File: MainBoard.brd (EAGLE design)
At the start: 0 parts

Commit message: Schematic for audio section
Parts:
- added C1, C10, C11, C2, C3, C4, C6, C7, C8, C9: 1µF, microbuilder:0805-NO
- added C5: 2.2u, microbuilder:0805-NO
- added J1: 22-27-2101-10, con-molex:6410-10
- added R1, R2: 10K, microbuilder:0805-NO
- added R3, R4, R5, R6: 100K, microbuilder:0805-NO
- added U1: microSD, SparkFun:MICRO-SD-SOCKET-PP
- added U2: TPA2016, tpa2016:S-PWQFN-N20
- added U3: AK4430ET, AK4430ET:16TSSOP
- added X1, X2, X3: 22-23-2021, con-molex:22-23-2021
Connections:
- new net +3V3: C10.2, C11.1, C3.2, C8.2, R1.1, R2.2, R3.2, R6.1, U1.1, U2.P$13, U3.P$11, U3.P$14
- new net AGND: C10.1, C4.1, C5.1, R4.1, R5.1, U2.P$14, U2.P$2, U2.P$3, U3.P$12
- new net GND: C11.2, C3.1, U1.6, U1.CD2, U1.GND1, U1.GND2, U2.P$21, U2.P$8
- new net I2SBICK: U3.P$5
- new net I2SLRCK: U3.P$7
- new net I2SMCLK: U3.P$4
- new net I2SSDTI: U3.P$6
- new net MMCCD: R6.2, U1.CD1
- new net MMCCS: U1.2
- new net MMCDI: U1.3
- new net MMCSCK: U1.5
- new net MMCSDO: U1.7
- new net MUTE: R1.2, R5.2, U2.P$18, U3.P$3
- new net N$1: U2.P$6, X1.1
- new net N$10: C8.1, C9.1, U3.P$15
- new net N$12: C9.2, U3.P$16
- new net N$13: C6.1, U3.P$1
- new net N$14: C6.2, U3.P$2
- new net N$15: R4.2, U3.P$8
- new net N$2: U2.P$7, X1.2
- new net N$3: U2.P$10, X2.1
- new net N$4: C2.1, U3.P$9
- new net N$5: C1.1, U3.P$10
- new net N$6: C1.2, U2.P$1
- new net N$7: C2.2, U2.P$15
- new net N$8: U2.P$9, X2.2
- new net N$9: C5.2, U3.P$13
- new net SCL: R2.1, U2.P$17
- new net SDA: R3.1, U2.P$19
- new net V+: C4.2, U2.P$11, U2.P$12, U2.P$4, U2.P$5
- new net VCC: U1.4

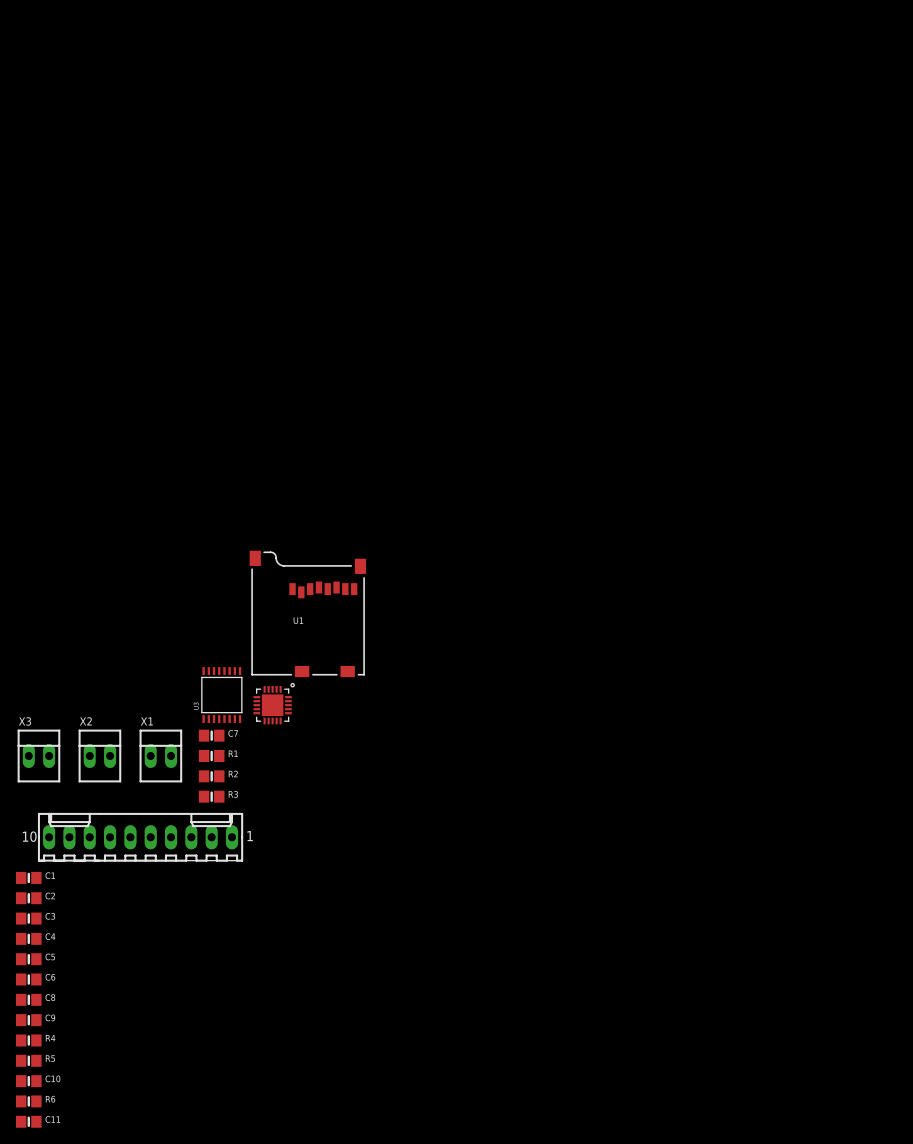
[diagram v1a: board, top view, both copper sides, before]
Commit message: Switched to SMT for power jack and headphones
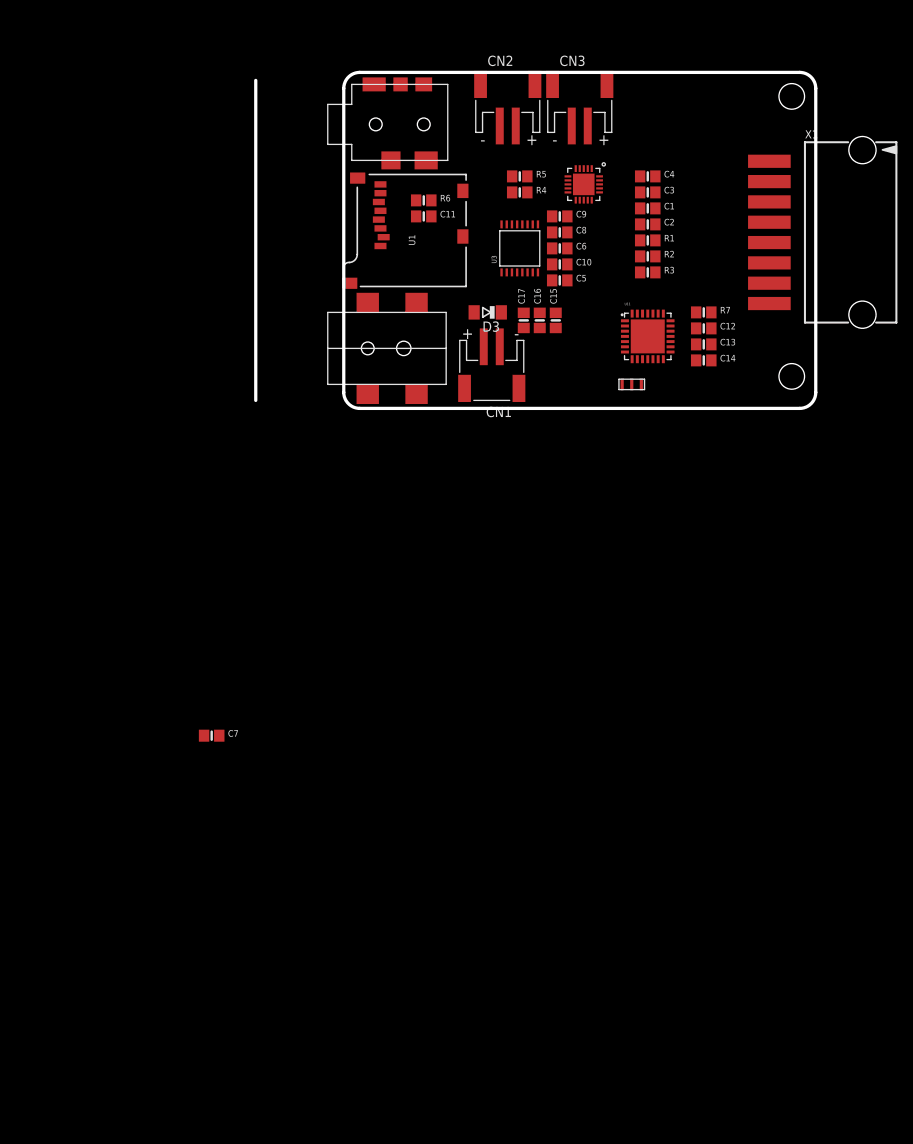
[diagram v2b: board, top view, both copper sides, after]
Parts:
- removed J1: 22-27-2101-10, con-molex:6410-10
- removed X2, X3: 22-23-2021, con-molex:22-23-2021
- added C12, C13, C14: 2.2u, microbuilder:0805-NO
- added C15, C16, C17: 1µF, microbuilder:0805-NO
- added CN1, CN2, CN3: (no value), adafruit:JST-PH-2-SMT-RA
- added D3: (no value), diode:SOD80C
- added R7: 100K, microbuilder:0805-NO
- added U$1: 3,5MMPHONO, sj1-351x:SJ1-351X
- added U$2: PJ-002AH, PJ-002AH-SMT:PJ-002AH-SMT
- added U11: PIC32MX110QFN, pic32mx110:28-QFN
- added U12: CSTCE, CSTCE:CSTCE
- X1: value 22-23-2021 -> C-GRID-08-15-91; device con-molex:22-23-2021 -> con-molex:15-91-08
- moved R5 126.4 mm to (22.0, 28.0)
- moved C11 123.5 mm to (10.0, 23.0)
- moved R6 123.0 mm to (10.0, 25.0)
- moved C4 122.8 mm to (38.0, 28.0)
- moved R4 122.5 mm to (22.0, 26.0)
- moved C10 121.8 mm to (27.0, 17.0)
- moved C9 120.4 mm to (27.0, 23.0)
- moved C3 119.3 mm to (38.0, 26.0)
- moved C8 116.7 mm to (27.0, 21.0)
- moved C2 114.4 mm to (38.0, 22.0)
- moved C1 114.0 mm to (38.0, 24.0)
- moved C6 112.9 mm to (27.0, 19.0)
- moved X1 108.8 mm to (64.0, 21.0), turned to 270 degrees
- moved C5 107.7 mm to (27.0, 15.0)
- moved R3 85.2 mm to (38.0, 16.0)
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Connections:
- new net !MCLR: R7.1, U11.P$26
- new net N$11: C13.2, U11.P$17
- new net N$16: U11.P$23
- new net N$17: U11.P$22
- new net N$18: U11.P$21
- new net N$19: U11.P$19
- new net N$20: U11.P$18
- new net N$21: U11.P$15
- new net N$22: U11.P$14
- new net N$24: U11.P$4
- new net N$25: U11.P$3
- new net N$26: U11.P$2
- new net N$27: U11.P$1
- new net N$28: U11.P$9
- new net N$29: U11.P$28
- new net N$31: CN1.2, U$2.3
- new net N$33: U$1.2, U3.P$10
- new net N$34: U$1.3, U3.P$9
- new net N$36: CN1.1, D3.A, U$2.1, U$2.A
- new net PGC: U11.P$12
- new net PGD: U11.P$11
- new net RIRQ: X1.5
- new net RMISO: X1.4
- new net RMOSI: X1.3
- new net RRST: X1.7
- new net RSCK: X1.2
- new net RSDA: X1.1
- new net XI: U11.P$6, U12.3
- new net XO: U11.P$7, U12.1
- net +3V3: now also C12.2, C14.2, R7.2, U11.P$16, U11.P$5, X1.8
- net AGND: now also C15.1, C16.1, C17.1, U$1.1, U$2.2
- net GND: now also C12.1, C13.1, C14.1, U11.P$10, U11.P$24, U11.P$25, U11.P$29, U12.2, X1.6
- net N$1: now also CN2.1; no longer X1.1
- net N$2: now also CN2.2; no longer X1.2
- net N$3: now also CN3.1; no longer X2.1
- net N$4: now also U$1.5; no longer U3.P$9
- net N$5: now also U$1.4; no longer U3.P$10
- net N$8: now also CN3.2; no longer X2.2
- net VCC: now also C15.2, C16.2, C17.2, D3.C
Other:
- board outline added: 70 x 42 mm

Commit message: More routing
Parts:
- removed C3, C7, C8: 1µF, microbuilder:0805-NO
- added C18: 1µF, microbuilder:0805-NO
- added C21: 10pF, microbuilder:0603-NO
- added C22, C23, C24: 22uF/10V X5R, microbuilder:0805-NO
- added C25: 1uF/10V X5R, microbuilder:0805-NO
- added L1: NRS5030T1R0NMGJ, microbuilder:INDUCTOR_5X5MM_TDK_VLC5045
- added R12, R13, R9: 105K, microbuilder:0603-NO
- added R8: 1M, microbuilder:0603-NO
- added RN1: (no value), resistor-dil:4X0402ARV341
- added U$3: JST-4PIN, adafruit:JST-PH-4-SMT-RA
- added U4: TPS63060, microbuilder:PWSON-N10
- added X2: 22-23-2051, con-molex:22-23-2051
- C1, C10, C11, C12, C13, C14, C2, C5, C6, C9, R1, R2, R3, R4, R5, R6, R7: device microbuilder:0805-NO -> microbuilder:0603-NO
- moved C12 30.2 mm to (16.7, 19.4), turned to 90 degrees
- moved R7 28.0 mm to (22.6, 27.8), turned to 90 degrees
- moved CN2 25.0 mm to (45.5, 37.0)
- moved U12 24.6 mm to (18.3, 19.1), turned to 270 degrees
- moved C5 22.6 mm to (16.2, 34.9)
- moved C14 22.1 mm to (29.0, 20.3), turned to 180 degrees
- moved C13 21.8 mm to (29.0, 21.8), turned to 180 degrees
- moved U11 20.5 mm to (23.3, 22.3)
- moved C10 19.6 mm to (16.2, 33.4)
- moved U3 16.4 mm to (22.7, 35.4), turned to 90 degrees
- moved C11 14.8 mm to (16.2, 36.4), turned to 180 degrees
- moved C9 14.0 mm to (16.2, 31.9)
- moved C6 13.2 mm to (28.7, 32.1)
- moved R4 11.5 mm to (28.7, 35.4), turned to 180 degrees
- moved U2 10.9 mm to (40.9, 26.0), turned to 270 degrees
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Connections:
- net N$33 renamed AOUTL
- net N$34 renamed AOUTR
- removed net MMCDI: U1.3
- removed net MMCSDO: U1.7
- removed net N$17: U11.P$22
- removed net N$19: U11.P$19
- removed net N$20: U11.P$18
- removed net N$21: U11.P$15
- removed net N$22: U11.P$14
- removed net N$24: U11.P$4
- removed net N$25: U11.P$3
- removed net N$27: U11.P$1
- removed net N$28: U11.P$9
- removed net N$29: U11.P$28
- removed net RMISO: X1.4
- removed net RMOSI: X1.3
- removed net RSCK: X1.2
- removed net RSDA: X1.1
- removed net V+: C4.2, U2.P$11, U2.P$12, U2.P$4, U2.P$5
- new net ENABLE: R12.2, U4.3
- new net N$30: L1.P$2, U4.10
- new net N$32: U4.6
- new net N$33: C21.1, R8.1, R9.2, U4.8
- new net PS: R13.1, U4.4
- new net RFIDSS: U11.P$19, X1.1
- new net SDI: U1.7, U11.P$2, X1.4
- new net SDO: U1.3, U11.P$3, X1.3
- net !MCLR: now also X2.1
- net +3V3: now also C18.2, C22.1, C23.1, C24.1, C25.1, C4.2, R8.2, U$3.3, U2.P$11, U2.P$12, U2.P$4, U2.P$5, U4.9; no longer C3.2, C8.2
- net AGND: no longer C10.1, C15.1, C16.1, C17.1, C4.1, C5.1, R5.1, U$1.1, U$2.2, U2.P$14, U2.P$2, U2.P$3, U3.P$12
- net GND: now also C10.1, C15.1, C16.1, C17.1, C18.1, C21.2, C22.2, C23.2, C24.2, C25.2, C4.1, C5.1, C9.1, R13.2, R5.1, R9.1, U$1.1, U$2.2, U$3.4, U2.P$14, U2.P$2, U2.P$3, U3.P$12, U3.P$15, U4.7, U4.THERMAL@1, U4.THERMAL@10, U4.THERMAL@11, U4.THERMAL@12, U4.THERMAL@13, U4.THERMAL@14, U4.THERMAL@5, U4.THERMAL@6, U4.THERMAL@7, U4.THERMAL@8, U4.THERMAL@9, X2.3; no longer C3.1
- net I2SBICK: now also RN1.3, RN1.6, U11.P$23
- net I2SLRCK: now also RN1.1, RN1.8, U11.P$18
- net I2SMCLK: now also RN1.4, RN1.5, U11.P$28
- net I2SSDTI: now also RN1.2, RN1.7, U11.P$9
- net MMCCD: now also U11.P$1
- net MMCCS: now also U11.P$4
- net MMCSCK: now also U11.P$22, X1.2
- net N$10: now also L1.P$1, U4.1; no longer C8.1, C9.1, U3.P$15
- net N$16: now also U11.P$20; no longer U11.P$23
- net N$26: now also U11.P$27; no longer U11.P$2
- net N$3: now also U2.P$9; no longer U2.P$10
- net N$8: now also U2.P$10; no longer U2.P$9
- net PGC: now also X2.5
- net PGD: now also X2.4
- net RIRQ: now also U11.P$8
- net RRST: now also U11.P$13
- net SCL: now also U$3.2, U11.P$14
- net SDA: now also U$3.1, U11.P$15
- net VCC: now also R12.1, U4.2; no longer U1.4
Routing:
- net +3V3: track 0.00 -> 161.7 mm, vias 0 -> 14
- net SDI: track 0.00 -> 83.0 mm
- net GND: track 0.00 -> 81.5 mm, vias 0 -> 79
- net SDO: track 0.00 -> 79.5 mm
- net MMCSCK: track 0.00 -> 68.1 mm, vias 0 -> 5
- net N$5: track 0.00 -> 49.4 mm, vias 0 -> 2
- net MUTE: track 0.00 -> 47.5 mm, vias 0 -> 9
- net N$4: track 0.00 -> 44.3 mm, vias 0 -> 2
- net SDA: track 0.00 -> 43.3 mm, vias 0 -> 7
- net RIRQ: track 0.00 -> 42.0 mm, vias 0 -> 2
- net SCL: track 0.00 -> 38.8 mm, vias 0 -> 8
- net RFIDSS: track 0.00 -> 38.1 mm, vias 0 -> 2
- net !MCLR: track 0.00 -> 34.8 mm, vias 0 -> 2
- net RRST: track 0.00 -> 33.5 mm, vias 0 -> 2
- net I2SSDTI: track 0.00 -> 31.8 mm, vias 0 -> 2
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- added copper zone on layer 1, net GND
- added copper zone on layer 16, net GND

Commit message: copper done
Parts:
- removed RN1: (no value), resistor-dil:4X0402ARV341
- added R10, R11: 105K, microbuilder:0603-NO
- moved C12 0.35 mm to (16.7, 19.1)
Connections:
- net N$16 renamed VSENSE
- removed net N$18: U11.P$21
- removed net N$26: U11.P$27
- new net BATS: R10.1, R11.2, U11.P$27
- net +3V3: now also U1.4; no longer U1.1
- net GND: now also R11.1
- net I2SBICK: no longer RN1.3, RN1.6
- net I2SLRCK: no longer RN1.1, RN1.8
- net I2SMCLK: no longer RN1.4, RN1.5
- net I2SSDTI: no longer RN1.2, RN1.7
- net MUTE: now also U11.P$21
- net VCC: now also R10.2
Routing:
- net BATS: track 0.00 -> 25.2 mm, vias 0 -> 4
- net +3V3: track 161.7 -> 169.6 mm, vias 14 -> 16
- net VCC: track 15.8 -> 18.5 mm
- net !MCLR: track 34.8 -> 37.1 mm
- net I2SSDTI: track 31.8 -> 34.0 mm
- net MMCSCK: track 68.1 -> 69.4 mm
- net I2SLRCK: track 21.8 -> 22.9 mm, vias 0 -> 2
- net I2SBICK: track 11.0 -> 12.0 mm
- net GND: track 81.5 -> 81.4 mm, vias 79 -> 80
